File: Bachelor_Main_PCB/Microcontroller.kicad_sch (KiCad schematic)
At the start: 2 parts, among them U3 STM32H7A3ZITxQ, U4 USB3320C-EZK-TR

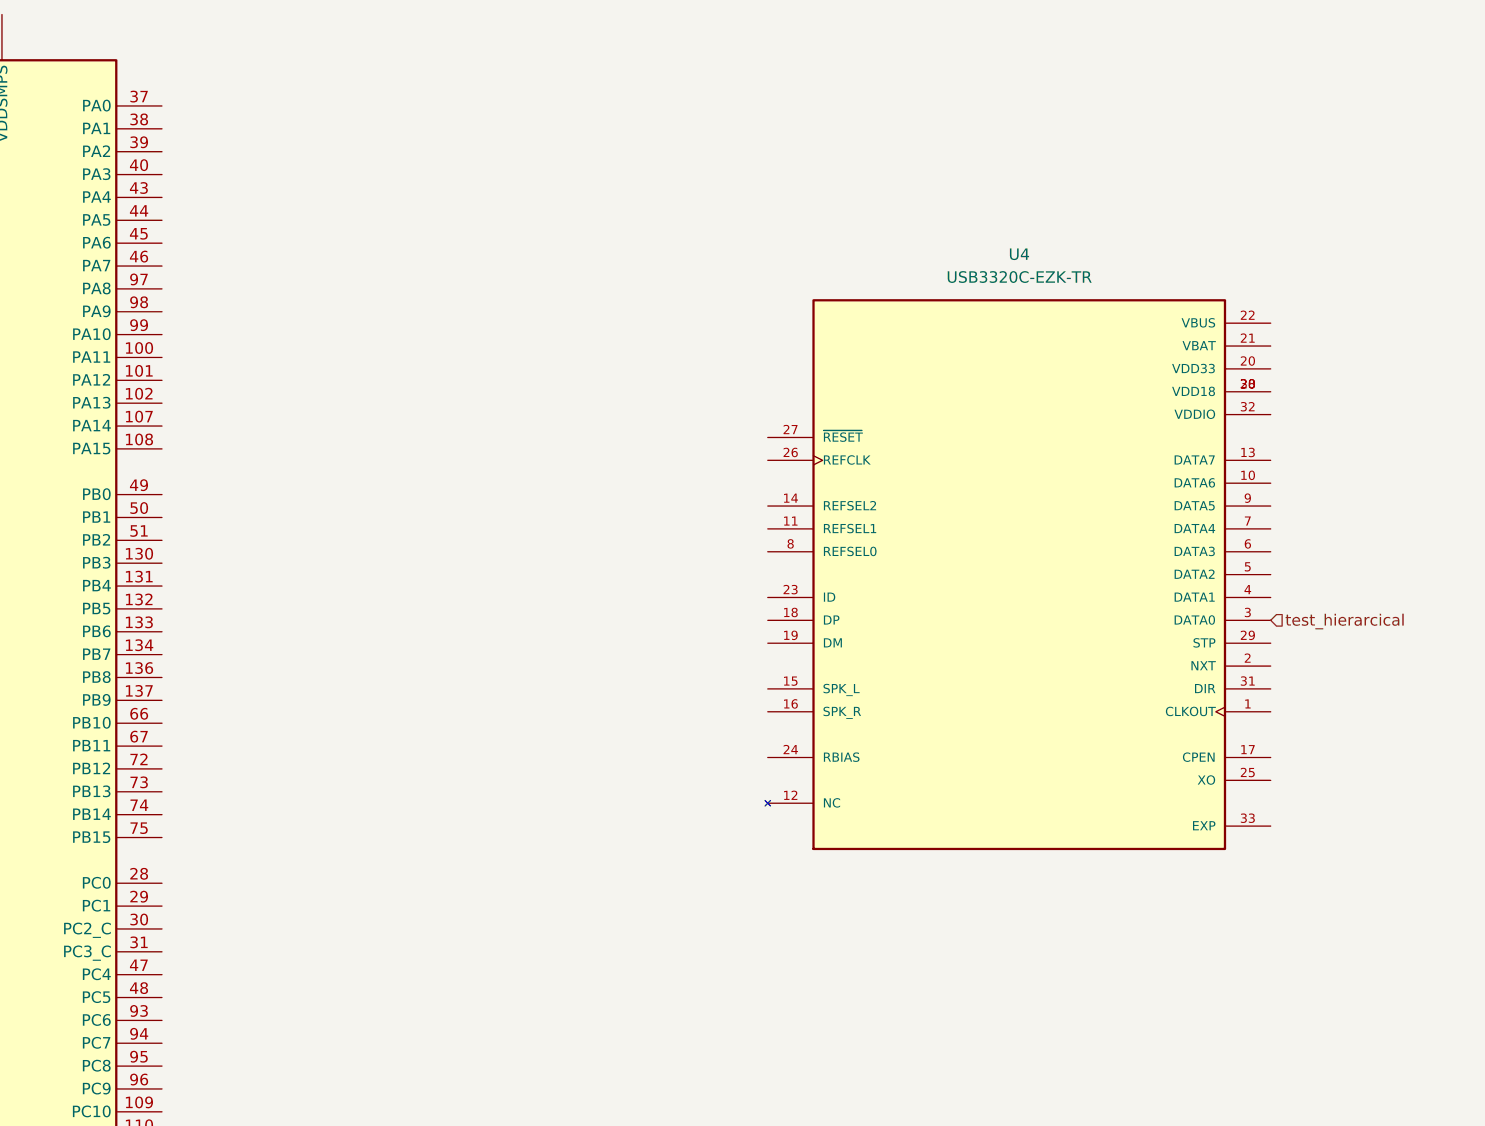
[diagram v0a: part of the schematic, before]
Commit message: Routed all 12ULPI pins to MCU
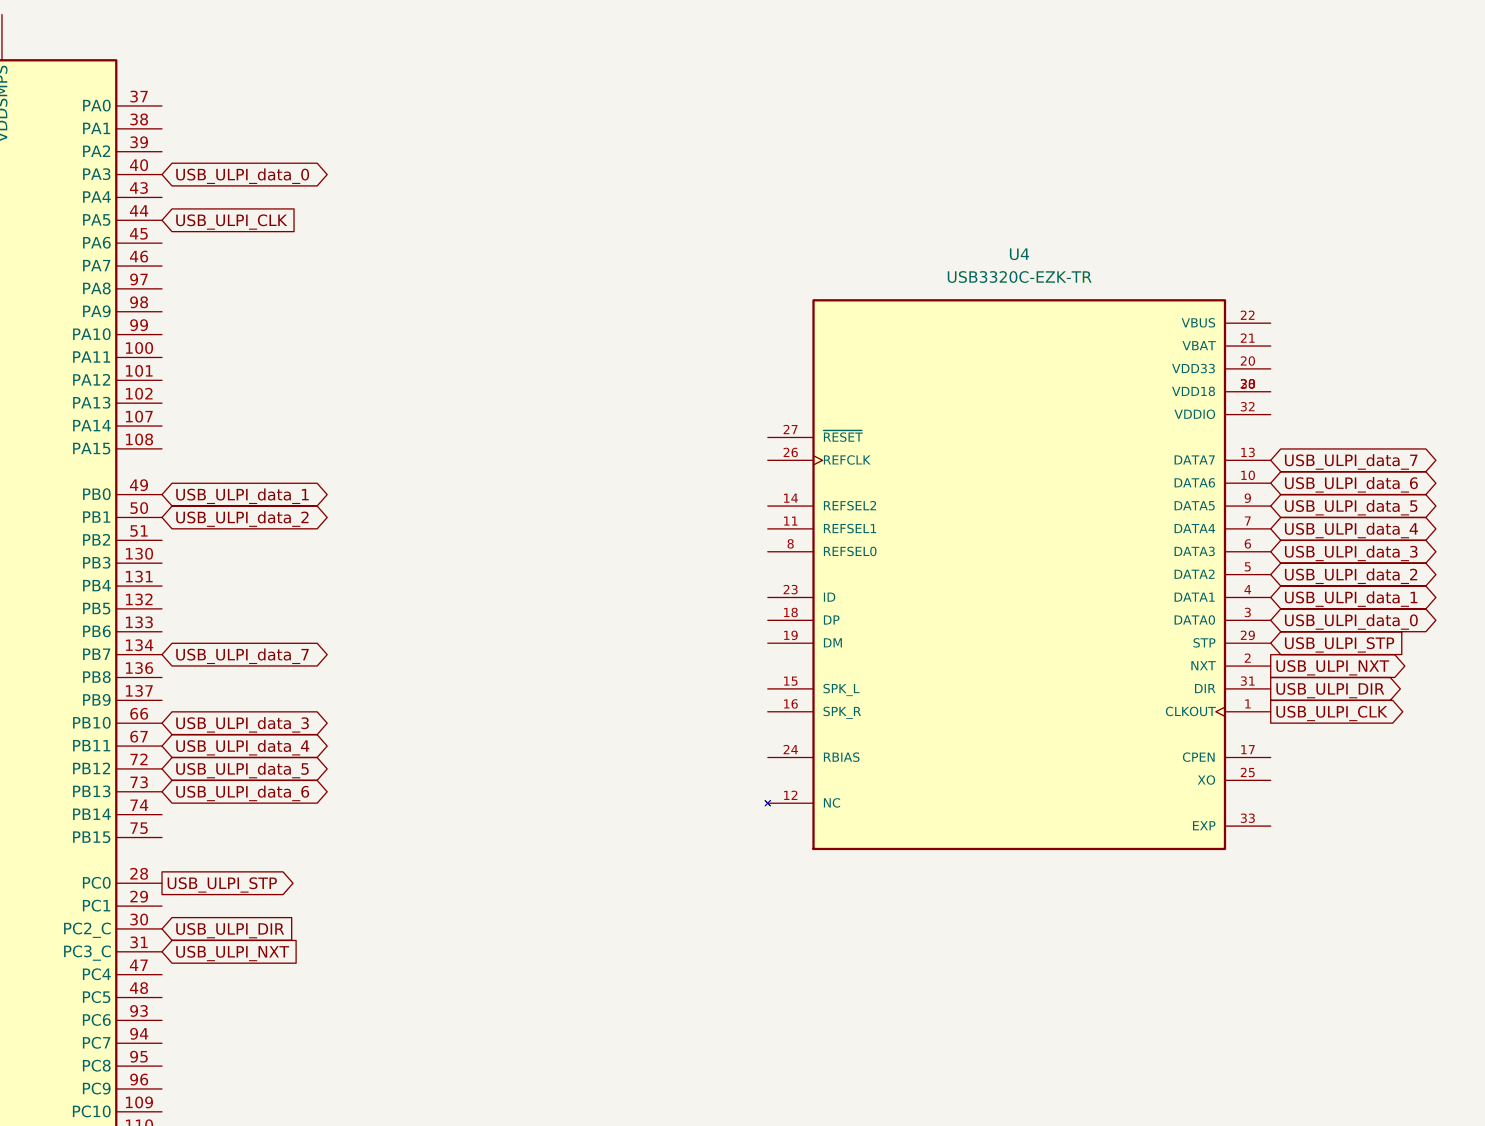
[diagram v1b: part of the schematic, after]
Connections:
- net test_hierarcical is gone; now on net USB_ULPI_data_0: U4.3 (DATA0)
- net USB_ULPI_data_7: now reaches U3.134 (PB7)
- net USB_ULPI_data_7: now also U4.13 (DATA7)
- net USB_ULPI_STP: now reaches U3.28 (PC0)
- net USB_ULPI_STP: now also U4.29 (STP)
- net USB_ULPI_DIR: now reaches U3.30 (PC2_C)
- net USB_ULPI_DIR: now also U4.31 (DIR)
- net USB_ULPI_NXT: now reaches U3.31 (PC3_C)
- net USB_ULPI_NXT: now also U4.2 (NXT)
- net USB_ULPI_data_0: now reaches U3.40 (PA3)
- net USB_ULPI_CLK: now reaches U3.44 (PA5)
- net USB_ULPI_CLK: now also U4.1 (CLKOUT)
- net USB_ULPI_data_1: now reaches U3.49 (PB0)
- net USB_ULPI_data_1: now also U4.4 (DATA1)
- net USB_ULPI_data_2: now reaches U3.50 (PB1)
- net USB_ULPI_data_2: now also U4.5 (DATA2)
- net USB_ULPI_data_3: now reaches U3.66 (PB10)
- net USB_ULPI_data_3: now also U4.6 (DATA3)
- net USB_ULPI_data_4: now reaches U3.67 (PB11)
- net USB_ULPI_data_4: now also U4.7 (DATA4)
- net USB_ULPI_data_5: now reaches U3.72 (PB12)
- net USB_ULPI_data_5: now also U4.9 (DATA5)
- net USB_ULPI_data_6: now reaches U3.73 (PB13)
- net USB_ULPI_data_6: now also U4.10 (DATA6)

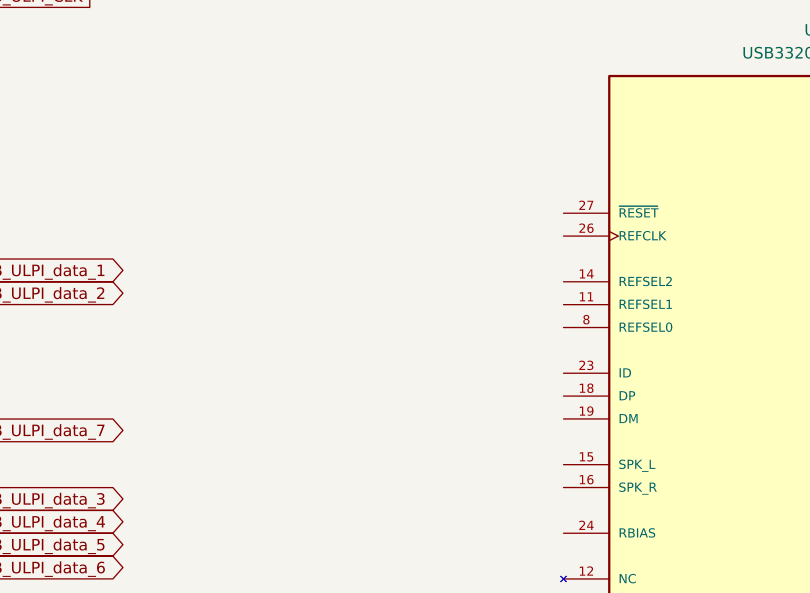
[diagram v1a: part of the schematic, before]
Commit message: Add Y1 oscillator to the USB3320
24Mhz oscillator for the USB tranciever
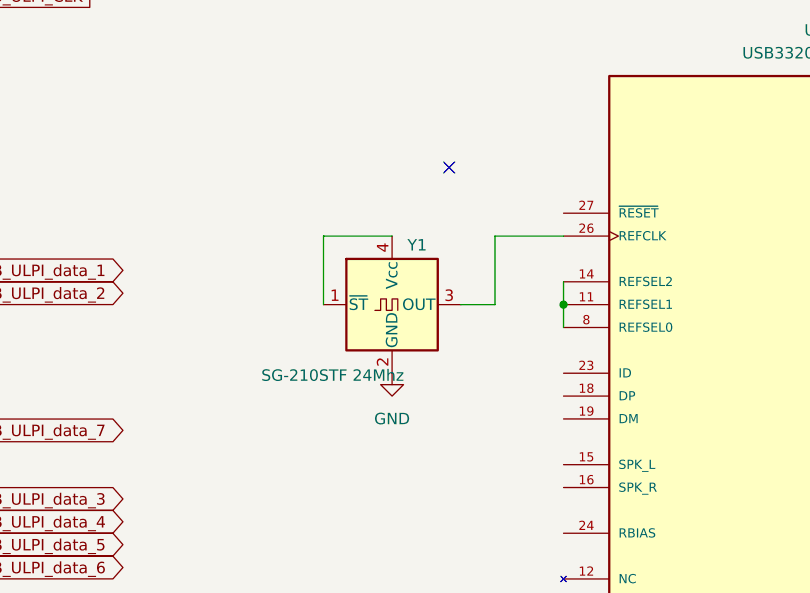
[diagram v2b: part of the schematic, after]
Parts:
- added Y1: SG-210STF 24Mhz, Oscillator:Oscillator_SMD_SeikoEpson_SG210-4Pin_2.5x2.0mm, symbol Oscillator:SG-210STF
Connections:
- net at U4.11 (REFSEL1): now also U4.14 (REFSEL2), U4.8 (REFSEL0)
- net at U4.26 (REFCLK): now also Y1.3 (OUT)
- new net: Y1.1 (~{ST}), Y1.4 (Vcc)
- new net GND: Y1.2 (GND)
- no-connect marks 0 -> 1
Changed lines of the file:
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@@
 	(generator_version "9.0")
 	(paper "A3")
+	(junction
+		(at 307.34 105.41)
+		(diameter 0)
+		(color 0 0 0 0)
+	)
+	(no_connect
+		(at 294.64 90.17)
+	)
+	(wire
+		(pts
+			(xy 299.72 105.41) (xy 299.72 97.79)
+		)
+		(stroke
+			(width 0)
+			(type default)
+		)
+	)
+	(wire
+		(pts
+			(xy 280.67 105.41) (xy 280.67 97.79)
+		)
+		(stroke
+			(width 0)
+			(type default)
+		)
+	)
+	(wire
+		(pts
+			(xy 295.91 105.41) (xy 299.72 105.41)
+		)
+		(stroke
+			(width 0)
+			(type default)
+		)
+	)
+	(wire
+		(pts
+			(xy 280.67 97.79) (xy 288.29 97.79)
+		)
+		(stroke
+			(width 0)
+			(type default)
+		)
+	)
+	(wire
+		(pts
+			(xy 299.72 97.79) (xy 307.34 97.79)
+		)
+		(stroke
+			(width 0)
+			(type default)
+		)
+	)
+	(wire
+		(pts
+			(xy 307.34 105.41) (xy 307.34 107.95)
+		)
+		(stroke
+			(width 0)
+			(type default)
+		)
+	)
+	(wire
+		(pts
+			(xy 307.34 102.87) (xy 307.34 105.41)
+		)
+		(stroke
+			(width 0)
+			(type default)
+		)
+	)
 	(global_label "USB_ULPI_STP"
 		(shape input)
@@
 				(justify left)
 				(hide yes)
+			)
+		)
+	)
+	(symbol
+		(lib_id "power:GND")
+		(at 288.29 113.03 0)
+		(unit 1)
+		(exclude_from_sim no)
+		(in_bom yes)
+		(on_board yes)
+		(dnp no)
+		(fields_autoplaced yes)
+		(property "Reference" "#PWR05"
+			(at 288.29 119.38 0)
+			(effects
+				(font
+					(size 1.27 1.27)
+				)
+				(hide yes)
+			)
+		)
+		(property "Value" "GND"
+			(at 288.29 118.11 0)
+			(effects
+				(font
+					(size 1.27 1.27)
+				)
+			)
+		)
+		(property "Footprint" ""
+			(at 288.29 113.03 0)
+			(effects
+				(font
+					(size 1.27 1.27)
+				)
+				(hide yes)
+			)
+		)
+		(property "Datasheet" ""
+			(at 288.29 113.03 0)
+			(effects
+				(font
+					(size 1.27 1.27)
+				)
+				(hide yes)
+			)
+		)
+		(property "Description" "Power symbol creates a global label with name \"GND\" , ground"
+			(at 288.29 113.03 0)
+			(effects
+				(font
+					(size 1.27 1.27)
+				)
+				(hide yes)
+			)
+		)
+		(pin "1"
+		)
+		(instances
+			(project ""
+				(path "/3544d663-329e-4884-b753-28436ca187e8/9cdc091d-5c59-45ee-8211-bdd0f330a333"
+					(reference "#PWR05")
+					(unit 1)
+				)
 			)
 		)
@@
 					(unit 1)
 				)
+			)
+		)
+	)
+	(symbol
+		(lib_id "Oscillator:SG-210STF")
+		(at 288.29 105.41 0)
+		(unit 1)
+		(exclude_from_sim no)
+		(in_bom yes)
+		(on_board yes)
+		(dnp no)
+		(property "Reference" "Y1"
+			(at 291.084 98.806 0)
+			(effects
+				(font
+					(size 1.27 1.27)
+				)
+			)
+		)
+		(property "Value" "SG-210STF 24Mhz"
+			(at 281.686 113.284 0)
+			(effects
+				(font
+					(size 1.27 1.27)
+				)
+			)
+		)
+		(property "Footprint" "Oscillator:Oscillator_SMD_SeikoEpson_SG210-4Pin_2.5x2.0mm"
+			(at 299.72 114.3 0)
+			(effects
+				(font
+					(size 1.27 1.27)
+				)
+				(hide yes)
+			)
+		)
+		(property "Datasheet" "https://support.epson.biz/td/api/doc_check.php?mode=dl&lang=en&Parts=SG-210STF"
+			(at 285.75 105.41 0)
+			(effects
+				(font
+					(size 1.27 1.27)
+				)
+				(hide yes)
+			)
+		)
+		(property "Description" "CMOS Crystal Oscillator SPXO"
+			(at 288.29 105.41 0)
+			(effects
+				(font
+					(size 1.27 1.27)
+				)
+				(hide yes)
+			)
+		)
+		(pin "1"
+		)
+		(pin "2"
+		)
+		(pin "3"
+		)
+		(pin "4"
+		)
+		(instances
+			(project ""
+				(path "/3544d663-329e-4884-b753-28436ca187e8/9cdc091d-5c59-45ee-8211-bdd0f330a333"
+					(reference "Y1")
+					(unit 1)
+				)

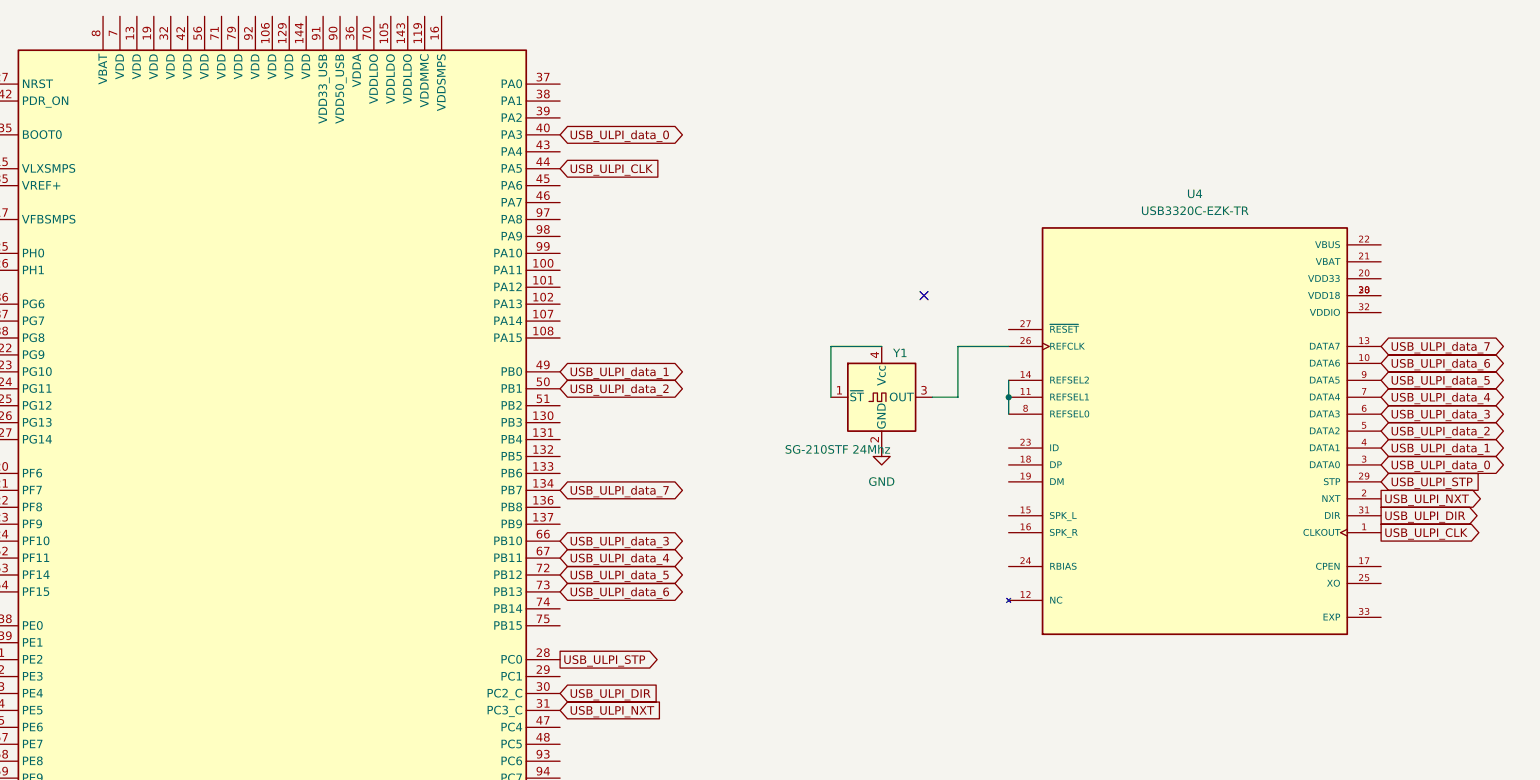
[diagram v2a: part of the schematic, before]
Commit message: Add Bypass cap USB3320
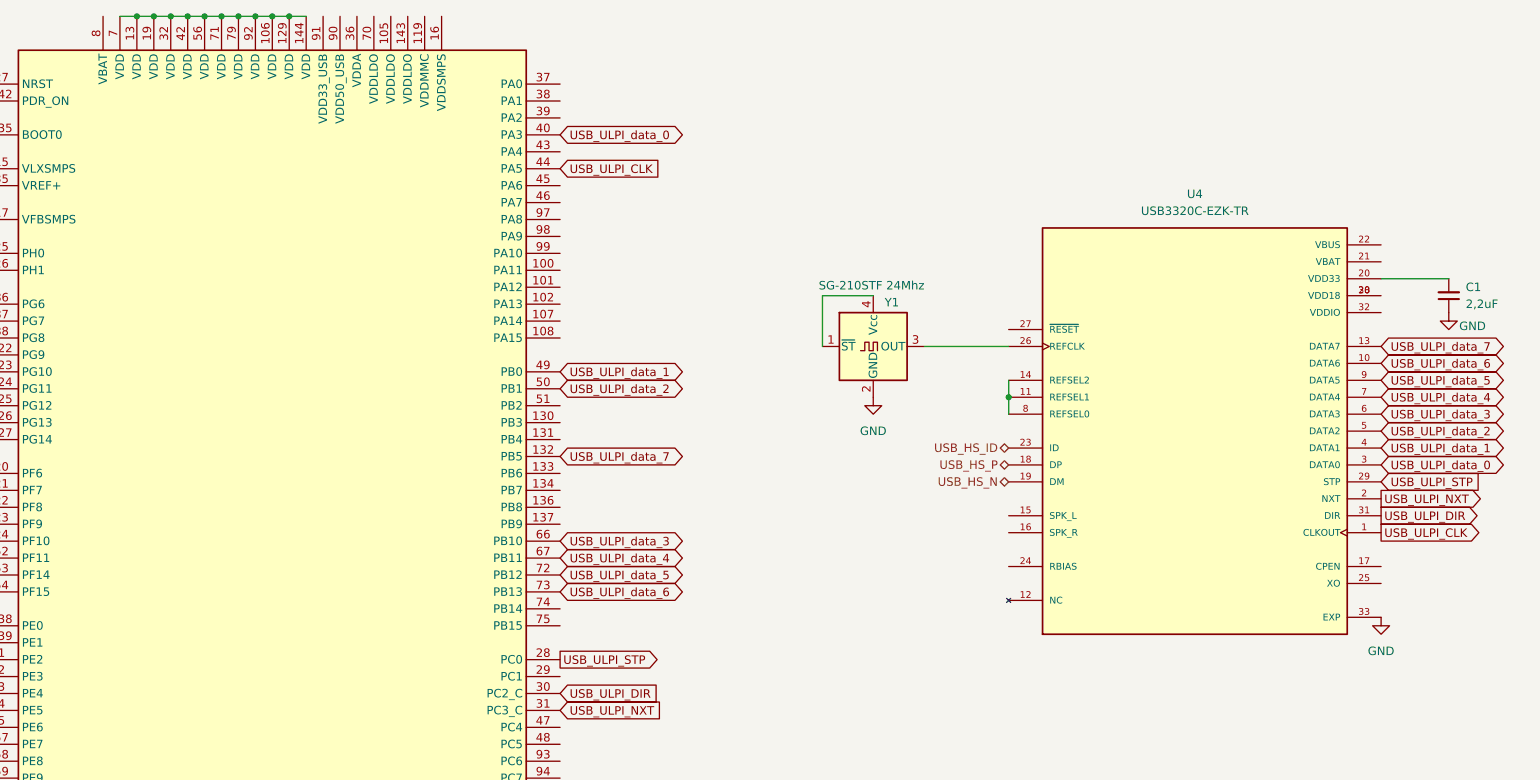
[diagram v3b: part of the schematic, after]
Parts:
- added C1: 2,2uF, Capacitor_SMD:C_0603_1608Metric, symbol Device:C_Small
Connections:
- net GND: now also U4.33 (EXP), C1.1
- net USB_ULPI_data_7: now also U3.132 (PB5); no longer U3.134 (PB7)
- net at U3.106 (VDD): now also U3.129 (VDD), U3.13 (VDD), U3.144 (VDD), U3.19 (VDD), U3.32 (VDD), U3.42 (VDD), U3.56 (VDD), U3.7 (VDD), U3.71 (VDD), U3.79 (VDD), U3.92 (VDD)
- net USB_HS_P: now reaches U4.18 (DP)
- net USB_HS_N: now reaches U4.19 (DM)
- net at U4.20 (VDD33): now also C1.2
- net USB_HS_ID: now reaches U4.23 (ID)
- no-connect marks 1 -> 0
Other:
- moved on the sheet: Y1

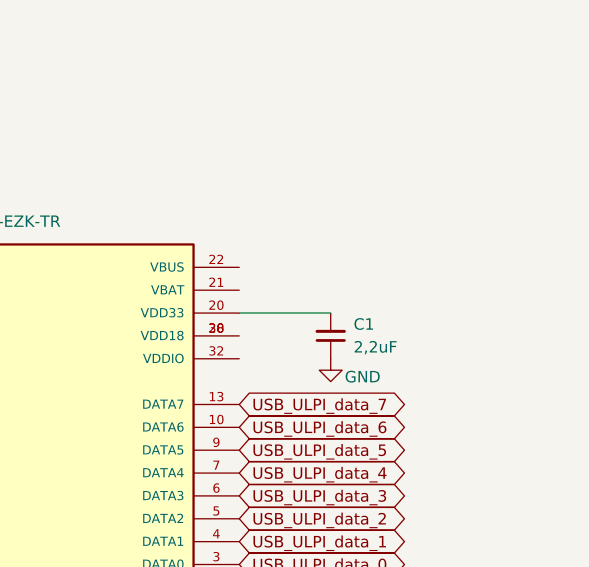
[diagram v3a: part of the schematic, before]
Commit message: Routing some MCU pins
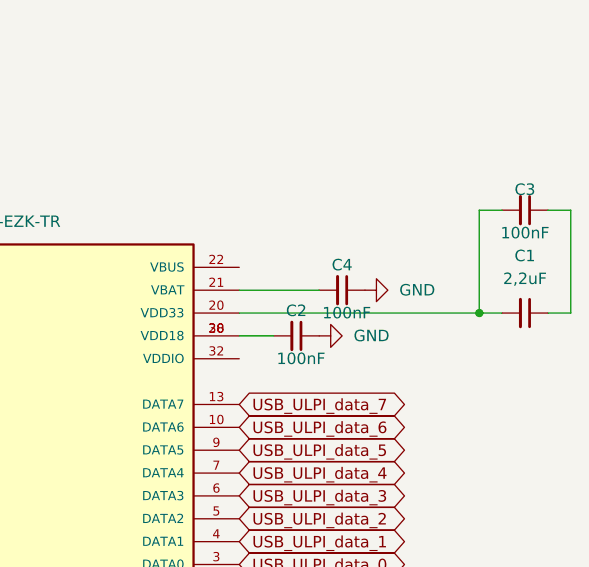
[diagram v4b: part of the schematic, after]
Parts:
- added C2, C3, C4: 100nF, Capacitor_SMD:C_0603_1608Metric, symbol Device:C_Small
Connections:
- net GND: now also C2.1, C4.1; no longer C1.1
- net at C1.2, U4.20 (VDD33): now also C3.2
- net at U4.21 (VBAT): now also C4.2
- net at U4.28 (VDD18), U4.30 (VDD18): now also C2.2
- new net: C1.1, C3.1
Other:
- moved on the sheet: C1
